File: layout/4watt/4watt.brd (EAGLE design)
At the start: 44.5 x 43.2 mm, 51 parts, among them IC2 FT232RL, P1 FSM4JSMA-SMD, Q1 IRF7413, Q2 IRF7413, Q3 IRF7413, Q4 IRF7413, T1 BC848, T2 BC848, T3 BC848, T4 BC848, T5 BC848, T6 BC848

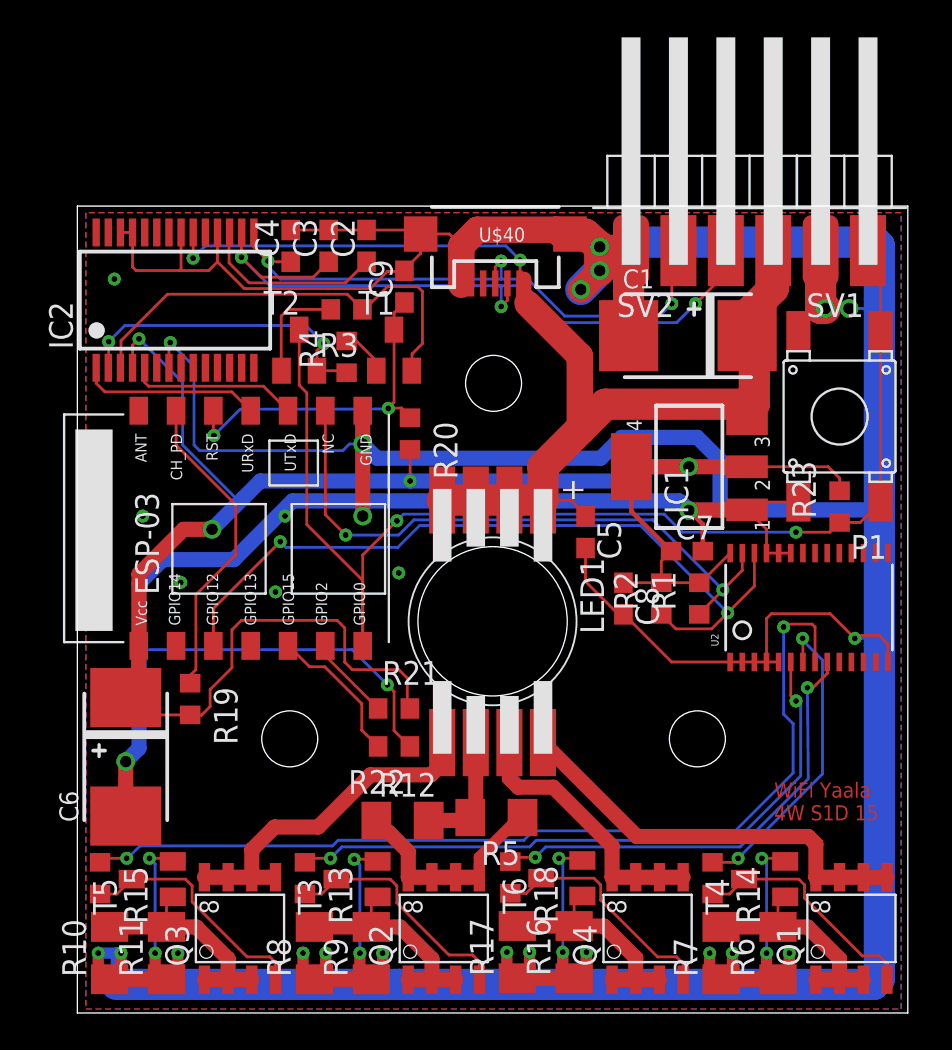
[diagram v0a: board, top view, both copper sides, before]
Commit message: ws28xx output and 2 additional RGBW led connectors
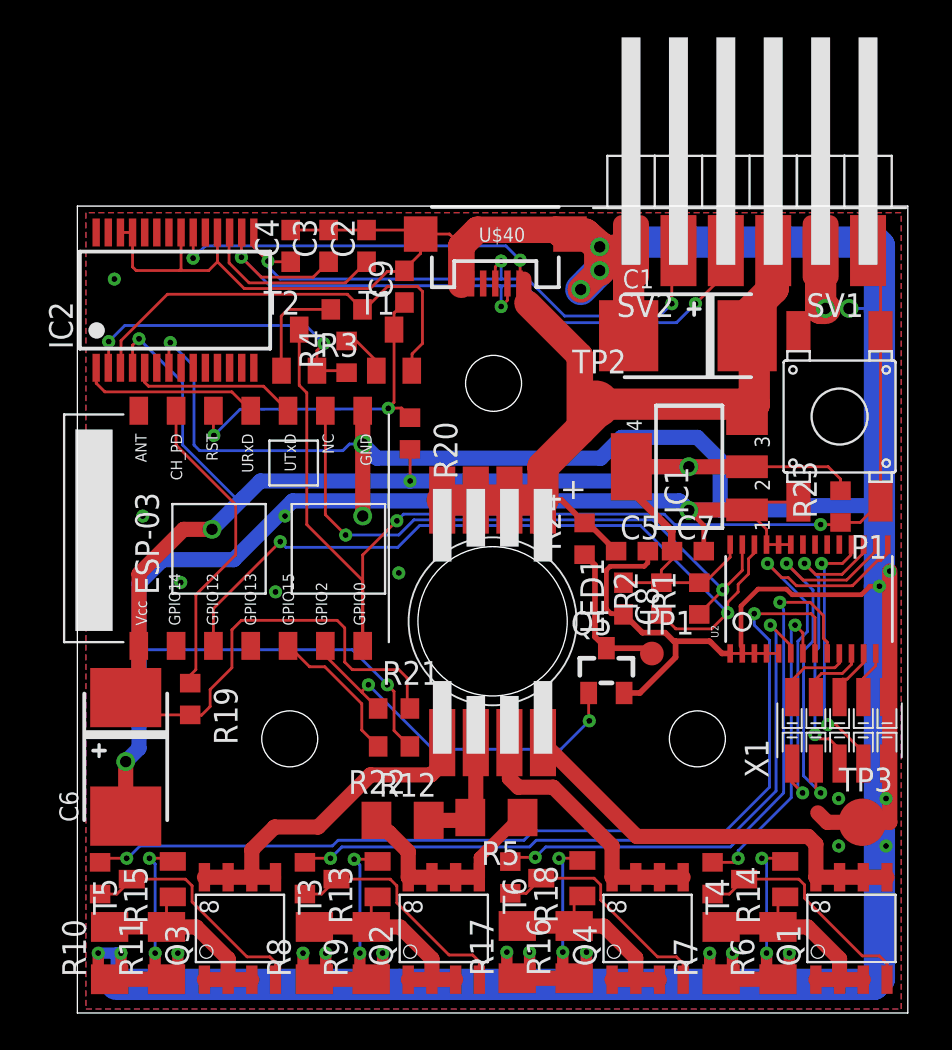
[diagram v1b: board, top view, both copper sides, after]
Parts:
- added Q5: BSS138, m-pad-2.1:SOT23
- added R24: 470, rcl-2:R0603
- added TP1: PTR1B1,27, testpad:B1,27
- added TP2, TP3: PTR1B2,54, testpad:B2,54
- added X1: 1296-T10, con-leotronics:1296-10
- moved C5 2.69 mm to (42.5, 38.8), turned to 0 degrees
- moved U2 0.46 mm to (52.0, 36.2)
- moved C7 0.05 mm to (45.5, 38.8)
- moved R23 0.05 mm to (53.6, 41.1)
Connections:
- new net GPIO2: Q5.1, R21.1, U$2.GPIO2
- new net N$15: U2.10, X1.2
- new net N$16: U2.11, X1.4
- new net N$17: U2.12, X1.6
- new net N$18: U2.13, X1.8
- new net N$19: U2.15, X1.1
- new net N$20: U2.16, X1.3
- new net N$21: U2.17, X1.5
- new net N$22: U2.18, X1.7
- net +5V: now also R24.2, TP2.TP
- net GND: now also Q5.2, TP3.TP, X1.10, X1.9
- net N$6: now also Q5.3, R24.1, TP1.TP; no longer R21.1, U$2.GPIO2
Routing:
- net GND: track 399.0 -> 425.4 mm, vias 38 -> 43
- net N$19: track 0.00 -> 23.4 mm, vias 0 -> 2
- net N$20: track 0.00 -> 21.3 mm, vias 0 -> 2
- net GPIO2: track 0.00 -> 20.5 mm, vias 0 -> 2
- net N$21: track 0.00 -> 16.3 mm, vias 0 -> 2
- net N$22: track 0.00 -> 14.2 mm, vias 0 -> 2
- net W: track 24.7 -> 31.2 mm
- net +5V: track 64.8 -> 70.1 mm
- net N$15: track 0.00 -> 4.34 mm
- net N$16: track 0.00 -> 3.78 mm
- net N$6: track 4.53 -> 8.05 mm
- net N$17: track 0.00 -> 3.02 mm
- net R: track 34.8 -> 37.8 mm
- net N$18: track 0.00 -> 2.61 mm
- net B: track 50.8 -> 52.4 mm
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
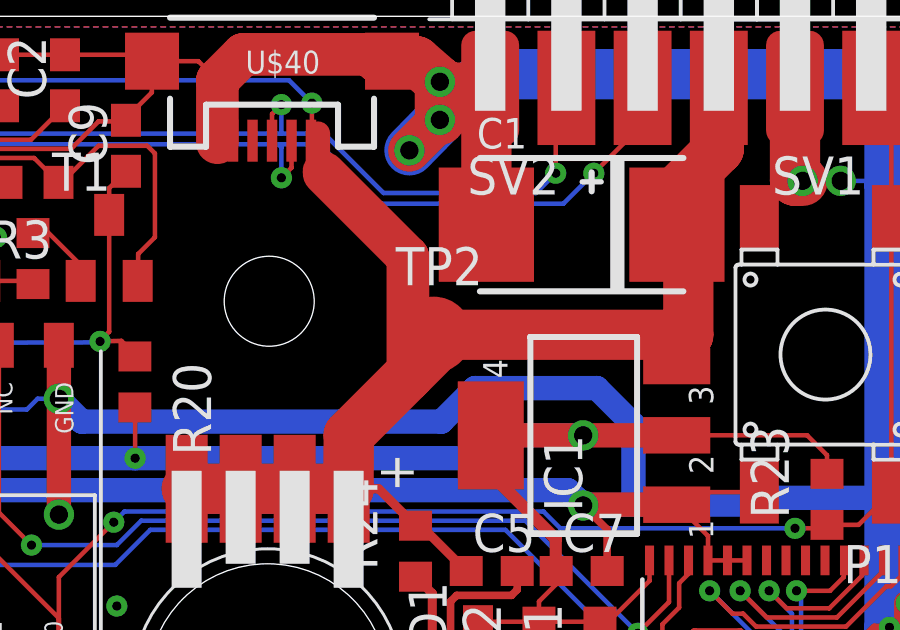
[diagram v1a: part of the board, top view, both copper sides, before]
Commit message: added doku layer
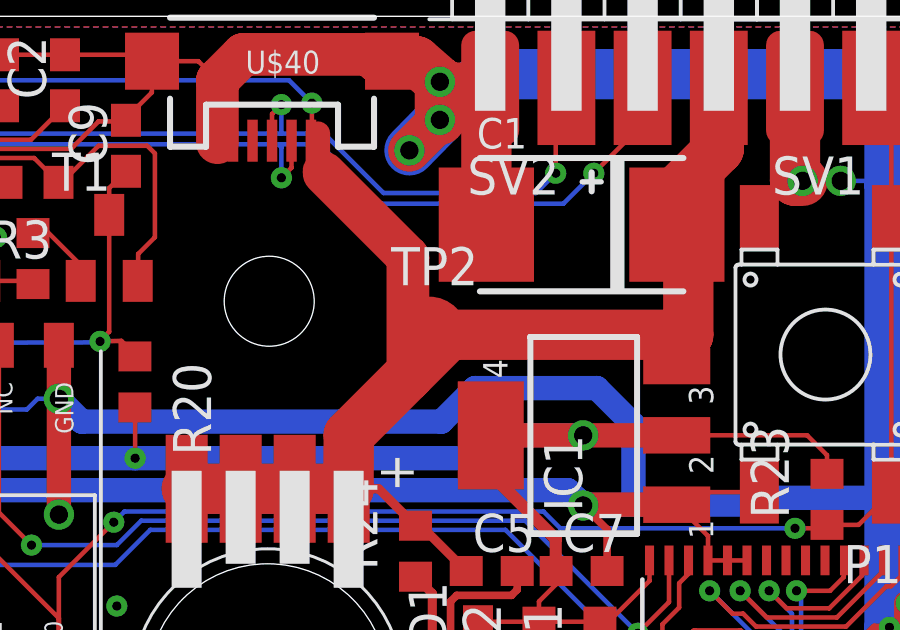
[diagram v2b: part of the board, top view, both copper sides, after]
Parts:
- moved TP2 0.15 mm to (40.4, 46.6)
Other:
- board text added: "+"
- board text added: "-"
- board text added: "1"
- board text added: "2"
- board text added: "WS"
- board text added: "v1.0"
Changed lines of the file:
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@@
 <layer number="22" name="bPlace" color="7" fill="1" visible="yes" active="yes"/>
 <layer number="23" name="tOrigins" color="15" fill="1" visible="yes" active="yes"/>
-<layer number="24" name="bOrigins" color="15" fill="1" visible="yes" active="yes"/>
-<layer number="25" name="tNames" color="7" fill="1" visible="yes" active="yes"/>
+<layer number="24" name="bOrigins" color="15" fill="1" visible="no" active="yes"/>
+<layer number="25" name="tNames" color="7" fill="1" visible="no" active="yes"/>
 <layer number="26" name="bNames" color="7" fill="1" visible="no" active="yes"/>
 <layer number="27" name="tValues" color="7" fill="1" visible="no" active="yes"/>
@@
 <layer number="35" name="tGlue" color="7" fill="4" visible="no" active="yes"/>
 <layer number="36" name="bGlue" color="7" fill="5" visible="no" active="yes"/>
-<layer number="37" name="tTest" color="7" fill="1" visible="yes" active="yes"/>
+<layer number="37" name="tTest" color="7" fill="1" visible="no" active="yes"/>
 <layer number="38" name="bTest" color="7" fill="1" visible="no" active="yes"/>
 <layer number="39" name="tKeepout" color="4" fill="11" visible="yes" active="yes"/>
@@
 <layer number="41" name="tRestrict" color="4" fill="10" visible="yes" active="yes"/>
 <layer number="42" name="bRestrict" color="1" fill="10" visible="yes" active="yes"/>
-<layer number="43" name="vRestrict" color="2" fill="10" visible="yes" active="yes"/>
+<layer number="43" name="vRestrict" color="2" fill="10" visible="no" active="yes"/>
 <layer number="44" name="Drills" color="7" fill="1" visible="no" active="yes"/>
 <layer number="45" name="Holes" color="7" fill="1" visible="yes" active="yes"/>
@@
 <layer number="47" name="Measures" color="7" fill="1" visible="no" active="yes"/>
 <layer number="48" name="Document" color="7" fill="1" visible="yes" active="yes"/>
-<layer number="49" name="Reference" color="7" fill="1" visible="yes" active="yes"/>
+<layer number="49" name="Reference" color="7" fill="1" visible="no" active="yes"/>
 <layer number="50" name="dxf" color="7" fill="1" visible="no" active="no"/>
 <layer number="51" name="tDocu" color="7" fill="1" visible="yes" active="yes"/>
@@
 <wire x1="15.24" y1="46.736" x2="15.24" y2="32.766" width="0.254" layer="41"/>
 <wire x1="15.24" y1="32.766" x2="12.954" y2="32.766" width="0.254" layer="41"/>
-<text x="18.0848" y="22.9362" size="0.8128" layer="150" font="vector" ratio="20">WiFi Yaala
+<text x="18.0848" y="22.9362" size="0.9144" layer="48" font="vector" ratio="20">WiFi Yaala
 4W S1D 15</text>
 <rectangle x1="31.6992" y1="52.1208" x2="33.1724" y2="53.594" layer="29"/>
@@
 <vertex x="38.8112" y="53.4924"/>
 </polygon>
+<text x="44.6532" y="32.8422" size="0.9144" layer="48" font="vector" ratio="18">WS</text>
+<text x="52.451" y="24.13" size="0.9144" layer="48" font="vector" ratio="18">-</text>
+<text x="39.0144" y="44.6532" size="0.9144" layer="48" font="vector" ratio="18">+</text>
+<text x="49.9872" y="52.0446" size="0.9144" layer="48" font="vector" ratio="18">+</text>
+<text x="40.5892" y="52.3748" size="0.9144" layer="48" font="vector" ratio="18">-</text>
+<text x="49.5046" y="30.5816" size="0.9144" layer="48" font="vector" ratio="18">1</text>
+<text x="49.4538" y="26.6192" size="0.9144" layer="48" font="vector" ratio="18">2</text>
+<text x="18.0848" y="25.9842" size="0.9144" layer="48" font="vector" ratio="18">v1.0</text>
 </plain>
 <attributes>
@@
 <attribute name="TP_SIGNAL_NAME" value="" x="43.5356" y="33.274" size="1.778" layer="27" display="off"/>
 </element>
-<element name="TP2" library="testpad" package="B2,54" value="PTR1B2,54" x="40.5384" y="46.6344">
-<attribute name="TP_SIGNAL_NAME" value="" x="40.5384" y="46.6344" size="1.778" layer="27" display="off"/>
+<element name="TP2" library="testpad" package="B2,54" value="PTR1B2,54" x="40.386" y="46.6344">
+<attribute name="TP_SIGNAL_NAME" value="" x="40.386" y="46.6344" size="1.778" layer="27" display="off"/>
 </element>
 <element name="TP3" library="testpad" package="B2,54" value="PTR1B2,54" x="54.8132" y="24.2316">
@@
 <contactref element="TP2" pad="TP"/>
 <wire x1="39.6748" y1="45.2628" x2="39.6748" y2="44.6024" width="0.4064" layer="1"/>
-<wire x1="39.6748" y1="44.6024" x2="40.5384" y2="46.6344" width="0.4064" layer="1"/>
+<wire x1="39.6748" y1="44.6024" x2="40.386" y2="46.6344" width="0.4064" layer="1"/>
 <wire x1="37.7" y1="41.5" x2="38.6996" y2="41.5" width="0.3048" layer="1"/>
 <wire x1="38.6996" y1="41.5" x2="39.9288" y2="40.2708" width="0.3048" layer="1"/>

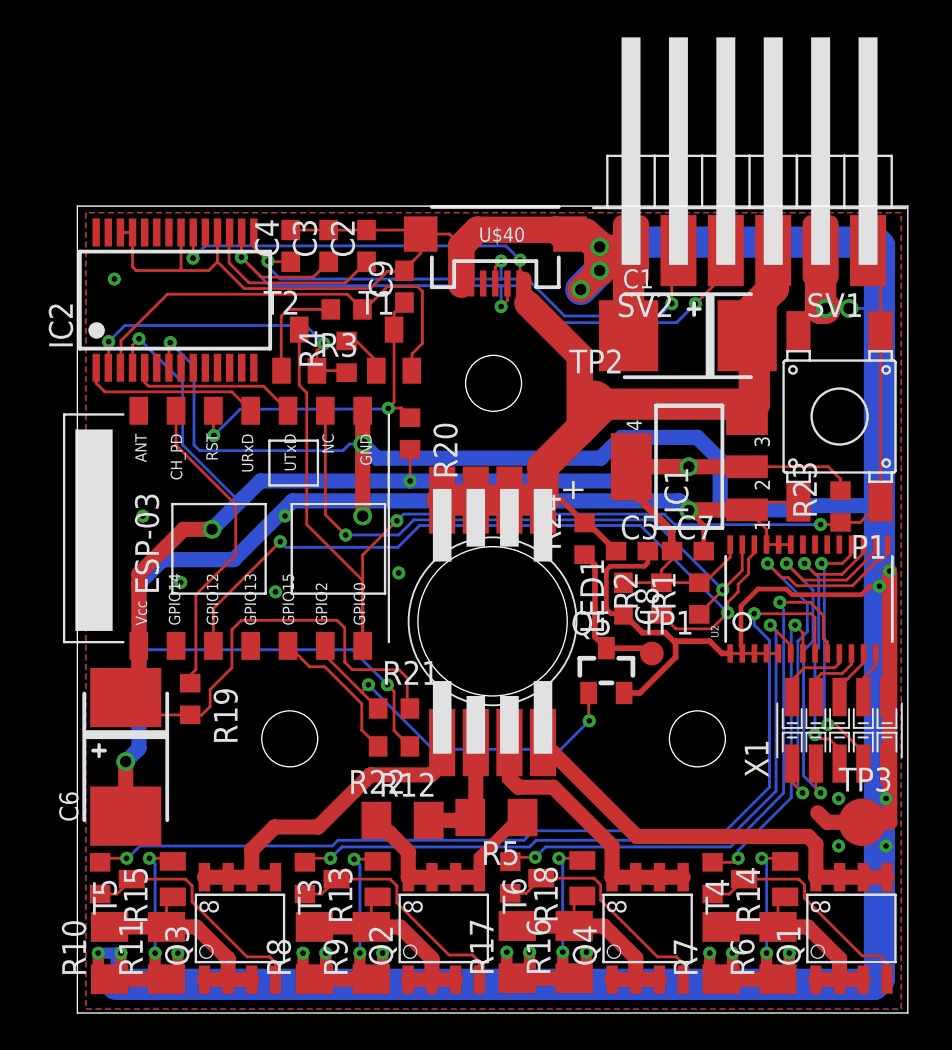
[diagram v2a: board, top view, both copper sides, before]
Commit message: Bauteilbeschriftung der Platinen base und 4watt geordnet. Bestückungspläne hinzugefügt.
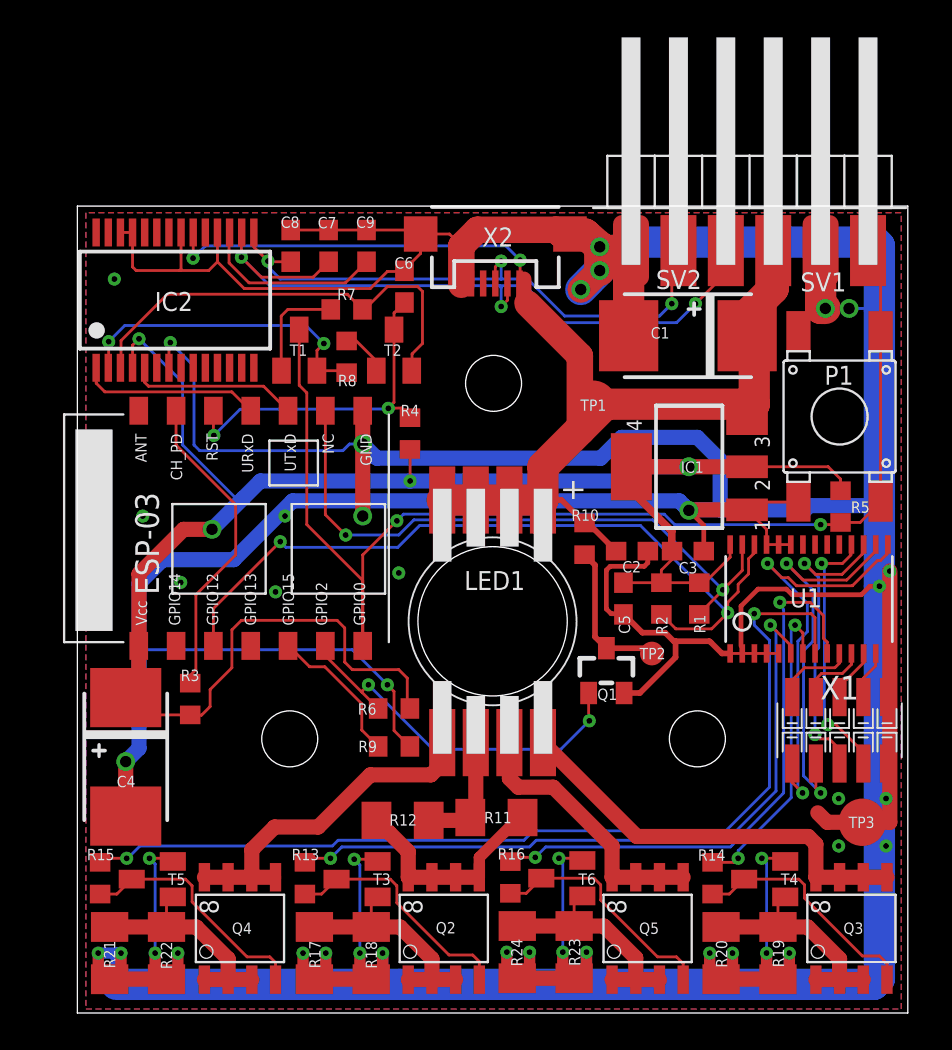
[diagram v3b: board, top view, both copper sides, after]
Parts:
- C3: value 22p -> 100n
- C4: value 22p -> 100u; device rcl:C0603 -> cap-master:7343-TE-D
- C6: value 100u -> 100n; device cap-master:7343-TE-D -> rcl:C0603
- C7, C8: value 100n -> 22p
- Q1: value IRF7413 -> BSS138; device transistor-fet:SO-8 -> m-pad-2.1:SOT23
- Q5: value BSS138 -> IRF7413; device m-pad-2.1:SOT23 -> transistor-fet:SO-8
- R10: value 3R6 -> 470; device rcl-2:M1206 -> rcl-2:R0603
- R16: value 3R6 -> 360; device rcl-2:M1206 -> rcl-2:R0603
- R18: value 360 -> 3R6; device rcl-2:R0603 -> rcl-2:M1206
- R19, R20, R21, R22, R23: value 10k -> 3R6; device rcl-2:R0603 -> rcl-2:M1206
- R24: value 470 -> 3R6; device rcl-2:R0603 -> rcl-2:M1206
- R5, R6, R7, R8, R9: value 3R6 -> 10k; device rcl-2:M1206 -> rcl-2:R0603
- TP1: value PTR1B1,27 -> PTR1B2,54; device testpad:B1,27 -> testpad:B2,54
- TP2: value PTR1B2,54 -> PTR1B1,27; device testpad:B2,54 -> testpad:B1,27
- moved R7 39.9 mm to (27.2, 51.7), turned to 180 degrees
- moved R19 34.3 mm to (50.3, 17.2), turned to 90 degrees
- moved R10 33.8 mm to (39.9, 39.4)
- moved Q3 32.8 mm to (53.6, 18.5)
- moved R20 32.5 mm to (47.2, 17.2), turned to 90 degrees
- moved R8 32.0 mm to (27.2, 49.2)
- moved C6 29.3 mm to (30.3, 52.9)
- moved C4 28.8 mm to (15.3, 27.7)
- moved R23 27.8 mm to (39.4, 17.3)
- moved C8 26.0 mm to (24.2, 55.1), turned to 90 degrees
- moved C3 25.3 mm to (45.5, 38.8), turned to 0 degrees
- moved C7 25.3 mm to (26.2, 55.1), turned to 90 degrees
- moved R5 24.9 mm to (53.6, 41.1), turned to 90 degrees
- moved R6 24.4 mm to (29.7, 30.3), turned to 0 degrees
- moved R3 22.5 mm to (18.8, 30.8), turned to 270 degrees
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- renumbered U$2 to U$1, U$40 to X2, U2 to U1
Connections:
- net +3V3: now also C3.1, C4.+, C5.1, R3.2, R4.2, R5.2, R6.2; no longer C6.+, C7.1, C8.1, R19.2, R20.2, R21.2, R23.2
- net +5V: now also C2.1, R10.2, TP1.TP; no longer C5.1, R24.2, TP2.TP
- net GND: now also C4.-, C6.2, Q1.2, R18.1, R19.1, R20.1, R21.1, R23.1, R24.1; no longer C4.2, C6.-, Q5.2, R10.1, R11.1, R16.1, R6.1, R7.1, R8.1
- net GPIO0: now also R5.1, T1.3; no longer R23.1, T2.3
- net GPIO15: now also R9.2; no longer R22.2
- net GPIO2: now also Q1.1, R6.1; no longer Q5.1, R21.1
- net N$1: now also R7.1, T2.2; no longer R3.1, T1.2
- net N$10: now also R11.1; no longer R5.1
- net N$11: now also Q5.4, R16.2; no longer Q4.4, R18.2
- net N$12: now also C9.1; no longer C2.1
- net N$13: now also Q5.1, Q5.2, Q5.3, R23.2, R24.2; no longer Q4.1, Q4.2, Q4.3, R16.2, R17.2
- net N$14: now also Q5.5, Q5.6, Q5.7, Q5.8; no longer Q4.5, Q4.6, Q4.7, Q4.8
- net N$2: now also R3.1; no longer R19.1
- net N$25: now also R11.2; no longer R5.2
- net N$26: now also Q3.4; no longer Q1.4
- net N$27: now also Q3.1, Q3.2, Q3.3, R19.2, R20.2; no longer Q1.1, Q1.2, Q1.3, R6.2, R7.2
- net N$28: now also Q3.5, Q3.6, Q3.7, Q3.8; no longer Q1.5, Q1.6, Q1.7, Q1.8
- net N$29: now also Q4.4; no longer Q3.4
- net N$3: now also C8.1; no longer C4.1
- net N$30: now also Q4.1, Q4.2, Q4.3, R21.2, R22.2; no longer Q3.1, Q3.2, Q3.3, R10.2, R11.2
- net N$31: now also Q4.5, Q4.6, Q4.7, Q4.8; no longer Q3.5, Q3.6, Q3.7, Q3.8
- net N$4: now also C7.1; no longer C3.1
- net N$5: now also R8.1, T1.2; no longer R4.1, T2.2
- net N$6: now also Q1.3, R10.1, TP2.TP; no longer Q5.3, R24.1, TP1.TP
- net N$7: now also R7.2, T1.1; no longer R3.2, T2.1
- net N$8: now also R8.2, T2.1; no longer R4.2, T1.1
- net N$9: now also R17.2, R18.2; no longer R8.2, R9.2
- net RST: now also C6.1, R4.1, T2.3; no longer C9.1, R20.1, T1.3
- net W: now also R16.1; no longer R18.1
